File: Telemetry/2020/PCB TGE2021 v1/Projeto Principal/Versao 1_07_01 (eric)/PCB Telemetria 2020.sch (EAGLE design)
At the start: 54 parts, among them IC1 INA240A1DR, IC2 MCP3221A6T-E_OTVAO, IC3 AZ1117IH-3.3TRG1, IC4 ACS758LCB-050B-PFF-T, IC5 ADS1115IDGSR, IC6 ACS712-030B3, IC7 THVD2410DR, IC8 TMP235AEDCKRQ1, J1 172042-0406, J2 43045-0412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

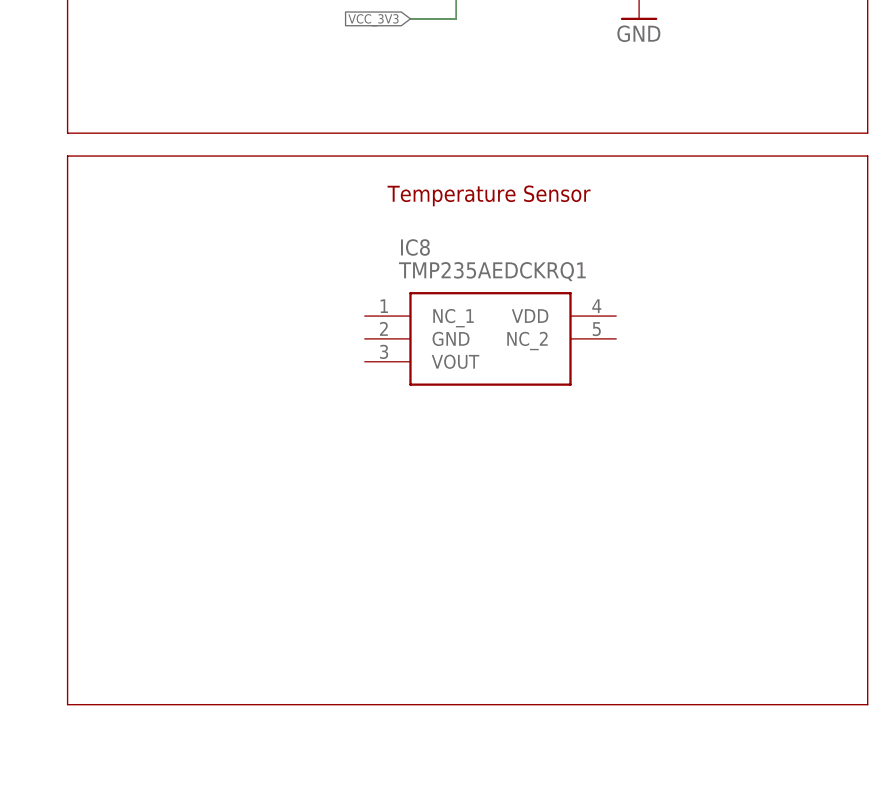
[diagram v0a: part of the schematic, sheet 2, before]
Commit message: Uploading TMP235 wiring
Extra connectors without wiring, that's the reason for V1.07.01
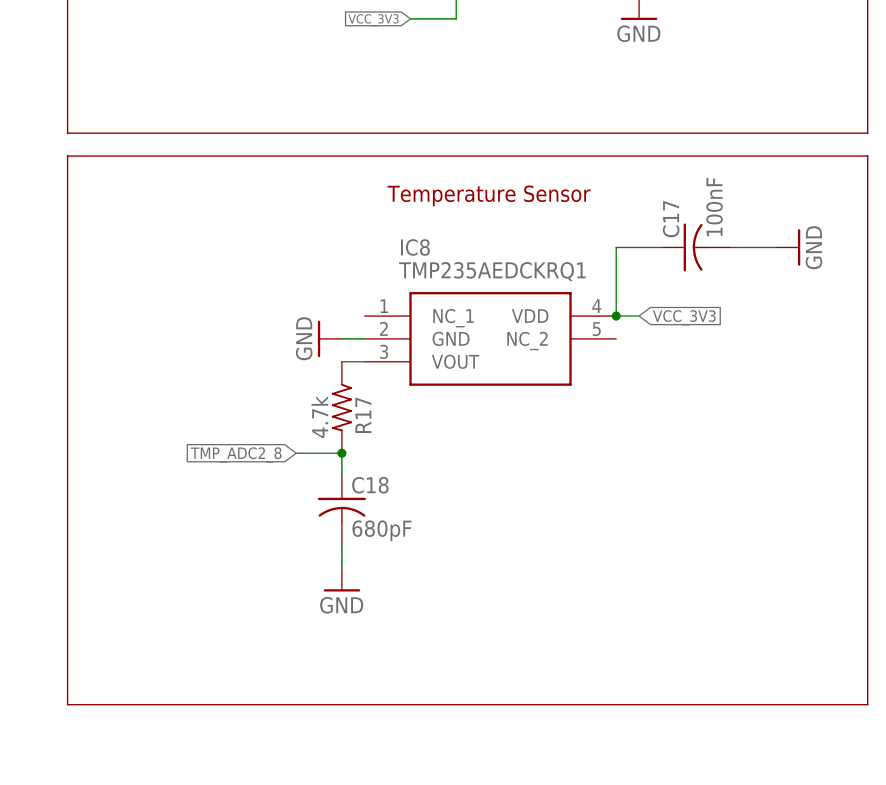
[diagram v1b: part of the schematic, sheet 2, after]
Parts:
- added C17: 100nF, rcl:C-USC0805
- added C18: 680pF, rcl:C-USC0805
- added R17: 4.7k, rcl:R-US_R0805
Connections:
- removed net N$11: U$1.14
- new net N$3: IC8.VOUT, R17.1
- new net TMP_ADC2_8: C18.1, R17.2, U$1.14
- net GND: now also C17.2, C18.2, IC8.GND
- net VCC_3V3: now also C17.1, IC8.VDD
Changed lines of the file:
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@@
 <?xml version="1.0" encoding="utf-8"?>
 <!DOCTYPE eagle SYSTEM "eagle.dtd">
-<eagle version="9.5.2">
+<eagle version="9.6.2">
 <drawing>
 <settings>
@@
 <part name="J5" library="SamacSys_Parts" deviceset="43045-0412" device=""/>
 <part name="IC8" library="SamacSys_Parts" deviceset="TMP235AEDCKRQ1" device=""/>
+<part name="GND14" library="supply1" library_urn="urn:adsk.eagle:library:371" deviceset="GND" device=""/>
+<part name="C17" library="rcl" library_urn="urn:adsk.eagle:library:334" deviceset="C-US" device="C0805" package3d_urn="urn:adsk.eagle:package:23617/2" value="100nF"/>
+<part name="GND18" library="supply1" library_urn="urn:adsk.eagle:library:371" deviceset="GND" device=""/>
+<part name="R17" library="rcl" library_urn="urn:adsk.eagle:library:334" deviceset="R-US_" device="R0805" package3d_urn="urn:adsk.eagle:package:23553/2" value="4.7k"/>
+<part name="C18" library="rcl" library_urn="urn:adsk.eagle:library:334" deviceset="C-US" device="C0805" package3d_urn="urn:adsk.eagle:package:23617/2" value="680pF"/>
+<part name="GND19" library="supply1" library_urn="urn:adsk.eagle:library:371" deviceset="GND" device=""/>
 </parts>
 <sheets>
@@
 </segment>
 </net>
-<net name="N$11" class="0">
+<net name="TMP_ADC2_8" class="0">
 <segment>
 <pinref part="U$1" gate="G$1" pin="14"/>
@@
 <attribute name="VALUE" x="321.31" y="129.54" size="1.778" layer="96" align="center-left"/>
 </instance>
+<instance part="GND14" gate="1" x="312.42" y="121.92" smashed="yes" rot="R270">
+<attribute name="VALUE" x="309.88" y="124.46" size="1.778" layer="96" rot="R270"/>
+</instance>
+<instance part="C17" gate="G$1" x="353.06" y="132.08" smashed="yes" rot="R90">
+<attribute name="NAME" x="352.425" y="133.096" size="1.778" layer="95" rot="R90"/>
+<attribute name="VALUE" x="357.251" y="133.096" size="1.778" layer="96" rot="R90"/>
+</instance>
+<instance part="GND18" gate="1" x="365.76" y="132.08" smashed="yes" rot="R90">
+<attribute name="VALUE" x="368.3" y="129.54" size="1.778" layer="96" rot="R90"/>
+</instance>
+<instance part="R17" gate="G$1" x="314.96" y="114.3" smashed="yes" rot="R270">
+<attribute name="NAME" x="316.4586" y="115.57" size="1.778" layer="95" rot="R270"/>
+<attribute name="VALUE" x="311.658" y="115.57" size="1.778" layer="96" rot="R270"/>
+</instance>
+<instance part="C18" gate="G$1" x="314.96" y="104.14" smashed="yes">
+<attribute name="NAME" x="315.976" y="104.775" size="1.778" layer="95"/>
+<attribute name="VALUE" x="315.976" y="99.949" size="1.778" layer="96"/>
+</instance>
+<instance part="GND19" gate="1" x="314.96" y="93.98" smashed="yes">
+<attribute name="VALUE" x="312.42" y="91.44" size="1.778" layer="96"/>
+</instance>
 </instances>
 <busses>
@@
 <wire x1="347.98" y1="160.02" x2="347.98" y2="162.56" width="0.1524" layer="91"/>
 </segment>
+<segment>
+<pinref part="GND14" gate="1" pin="GND"/>
+<pinref part="IC8" gate="G$1" pin="GND"/>
+<wire x1="314.96" y1="121.92" x2="317.5" y2="121.92" width="0.1524" layer="91"/>
+</segment>
+<segment>
+<pinref part="C17" gate="G$1" pin="2"/>
+<pinref part="GND18" gate="1" pin="GND"/>
+<wire x1="358.14" y1="132.08" x2="363.22" y2="132.08" width="0.1524" layer="91"/>
+</segment>
+<segment>
+<pinref part="C18" gate="G$1" pin="2"/>
+<pinref part="GND19" gate="1" pin="GND"/>
+<wire x1="314.96" y1="99.06" x2="314.96" y2="96.52" width="0.1524" layer="91"/>
+</segment>
 </net>
 <net name="VCC_3V3" class="0">
@@
 <label x="322.58" y="157.48" size="1.016" layer="95" rot="R180" xref="yes"/>
 <wire x1="327.66" y1="157.48" x2="322.58" y2="157.48" width="0.1524" layer="91"/>
+</segment>
+<segment>
+<pinref part="IC8" gate="G$1" pin="VDD"/>
+<wire x1="345.44" y1="124.46" x2="347.98" y2="124.46" width="0.1524" layer="91"/>
+<label x="347.98" y="124.46" size="1.27" layer="95" xref="yes"/>
+<pinref part="C17" gate="G$1" pin="1"/>
+<wire x1="350.52" y1="132.08" x2="345.44" y2="132.08" width="0.1524" layer="91"/>
+<wire x1="345.44" y1="132.08" x2="345.44" y2="124.46" width="0.1524" layer="91"/>
+<junction x="345.44" y="124.46"/>
 </segment>
 </net>
@@
 </segment>
 </net>
+<net name="N$3" class="0">
+<segment>
+<pinref part="R17" gate="G$1" pin="1"/>
+<pinref part="IC8" gate="G$1" pin="VOUT"/>
+<wire x1="314.96" y1="119.38" x2="317.5" y2="119.38" width="0.1524" layer="91"/>
+</segment>
+</net>
+<net name="TMP_ADC2_8" class="0">
+<segment>
+<pinref part="R17" gate="G$1" pin="2"/>
+<pinref part="C18" gate="G$1" pin="1"/>
+<wire x1="314.96" y1="109.22" x2="314.96" y2="106.68" width="0.1524" layer="91"/>
+<wire x1="314.96" y1="109.22" x2="309.88" y2="109.22" width="0.1524" layer="91"/>
+<junction x="314.96" y="109.22"/>
+<label x="309.88" y="109.22" size="1.27" layer="95" rot="R180" xref="yes"/>
+</segment>
+</net>
